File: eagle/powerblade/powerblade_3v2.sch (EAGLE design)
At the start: 78 parts, among them J1 JTAG_14PIN_IDC-ND, J2 AC_INF3, J4 TC2030-JLINK-NL, Q1 NTS4173, Q4 2SK1829, U1 TPS62122, U2 MCP6V3, U3 MSP430FR5738, U4 NRF51822QF, U6 MAX9910, U7 OPA2369, X1 16MHz, X3 32.768kHz, Y1 UREACH_XTEND

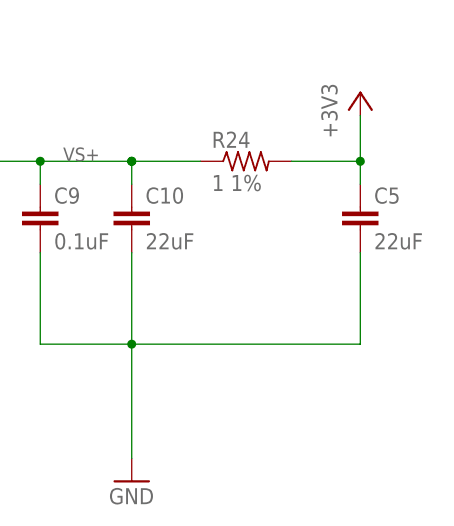
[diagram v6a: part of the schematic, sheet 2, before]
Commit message: updated most 0402 to new footprint
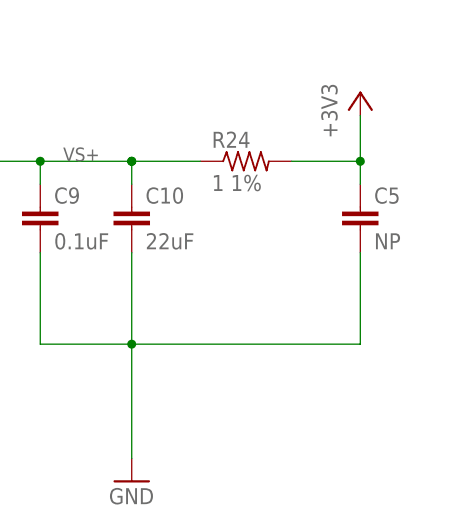
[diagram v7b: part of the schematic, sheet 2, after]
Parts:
- C11, C14, C16, C24, C27, C34, C38, C39, C4, C6, C7, C8: device rcl:C-EUC0402_SM -> rcl:C-EUC0402
- C5: value 22uF -> NP; DIGIKEY 445-9077-1-ND -> NP
- R14, R15, R16, R17, R18, R19, R35, R37, R38, R39, R40: device rcl:R-US_R0402_SM -> rcl:R-US_R0402
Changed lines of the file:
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@@
 <part name="GND3" library="supply1" deviceset="GND" device=""/>
 <part name="GND4" library="supply1" deviceset="GND" device=""/>
-<part name="C4" library="rcl" deviceset="C-EU" device="C0402_SM" value="22pF">
+<part name="C4" library="rcl" deviceset="C-EU" device="C0402" value="22pF">
 <attribute name="DIGIKEY" value="445-1239-1-ND"/>
 </part>
 <part name="P+2" library="supply1" deviceset="VCC" device=""/>
-<part name="C7" library="rcl" deviceset="C-EU" device="C0402_SM" value="4.7uF">
+<part name="C7" library="rcl" deviceset="C-EU" device="C0402" value="4.7uF">
 <attribute name="DIGIKEY" value="445-8023-1-ND"/>
 </part>
-<part name="C8" library="rcl" deviceset="C-EU" device="C0402_SM" value="0.1uF">
+<part name="C8" library="rcl" deviceset="C-EU" device="C0402" value="0.1uF">
 <attribute name="DIGIKEY" value="445-4952-1-ND"/>
 </part>
@@
 <attribute name="DIGIKEY" value="732-3452-1-ND"/>
 </part>
-<part name="R14" library="rcl" deviceset="R-US_" device="R0402_SM" value="200">
+<part name="R14" library="rcl" deviceset="R-US_" device="R0402" value="200">
 <attribute name="DIGIKEY" value="P200LCT-ND"/>
 </part>
-<part name="R15" library="rcl" deviceset="R-US_" device="R0402_SM" value="1M 1%">
-<attribute name="DIGIKEY" value="P1.00MLCT-ND"/>
-</part>
-<part name="R16" library="rcl" deviceset="R-US_" device="R0402_SM" value="75 1%">
+<part name="R15" library="rcl" deviceset="R-US_" device="R0402" value="1M 1%">
+<attribute name="DIGIKEY" value="P1.00MLCT-ND"/>
+</part>
+<part name="R16" library="rcl" deviceset="R-US_" device="R0402" value="75 1%">
 <attribute name="DIGIKEY" value="P75.0LCT-ND"/>
 </part>
-<part name="R17" library="rcl" deviceset="R-US_" device="R0402_SM" value="4.99k 1%">
+<part name="R17" library="rcl" deviceset="R-US_" device="R0402" value="4.99k 1%">
 <attribute name="DIGIKEY" value="P4.99KLCT-ND"/>
 <attribute name="DIGIKEY_2" value="P10.0KLCT-ND"/>
 </part>
-<part name="R18" library="rcl" deviceset="R-US_" device="R0402_SM" value="4.99 1%">
+<part name="R18" library="rcl" deviceset="R-US_" device="R0402" value="4.99 1%">
 <attribute name="DIGIKEY" value="RMCF0402FT4R99CT-ND"/>
 <attribute name="DIGIKEY_2" value="P10.0LCT-ND"/>
 </part>
-<part name="C27" library="rcl" deviceset="C-EU" device="C0402_SM" value="0.1uF">
+<part name="C27" library="rcl" deviceset="C-EU" device="C0402" value="0.1uF">
 <attribute name="DIGIKEY" value="445-4952-1-ND"/>
 </part>
@@
 <part name="+3V8" library="supply1" deviceset="+3V3" device=""/>
 <part name="U7" library="powerfilm" deviceset="OPA2369" device=""/>
-<part name="C38" library="rcl" deviceset="C-EU" device="C0402_SM" value="0.1uF">
+<part name="C38" library="rcl" deviceset="C-EU" device="C0402" value="0.1uF">
 <attribute name="DIGIKEY" value="445-4952-1-ND"/>
 </part>
 <part name="+3V3" library="supply1" deviceset="+3V3" device=""/>
-<part name="R35" library="rcl" deviceset="R-US_" device="R0402_SM" value="20k">
+<part name="R35" library="rcl" deviceset="R-US_" device="R0402" value="20k">
 <attribute name="DIGIKEY" value="P2.00KLCT-ND"/>
 <attribute name="DIGIKEY_2" value="P20.0KLCT-ND"/>
 </part>
-<part name="R37" library="rcl" deviceset="R-US_" device="R0402_SM" value="887k 1%">
+<part name="R37" library="rcl" deviceset="R-US_" device="R0402" value="887k 1%">
 <attribute name="DIGIKEY" value="P887KLCT-ND"/>
 </part>
-<part name="R38" library="rcl" deviceset="R-US_" device="R0402_SM" value="30k 1%">
+<part name="R38" library="rcl" deviceset="R-US_" device="R0402" value="30k 1%">
 <attribute name="DIGIKEY" value="P30.0KLCT-ND"/>
 </part>
-<part name="R40" library="rcl" deviceset="R-US_" device="R0402_SM" value="1M 1%">
-<attribute name="DIGIKEY" value="P1.00MLCT-ND"/>
-</part>
-<part name="C39" library="rcl" deviceset="C-EU" device="C0402_SM" value="1.5uF">
+<part name="R40" library="rcl" deviceset="R-US_" device="R0402" value="1M 1%">
+<attribute name="DIGIKEY" value="P1.00MLCT-ND"/>
+</part>
+<part name="C39" library="rcl" deviceset="C-EU" device="C0402" value="1.5uF">
 <attribute name="DIGIKEY" value="445-13815-1-ND"/>
 </part>
-<part name="R39" library="rcl" deviceset="R-US_" device="R0402_SM" value="16k 1%">
+<part name="R39" library="rcl" deviceset="R-US_" device="R0402" value="16k 1%">
 <attribute name="DIGIKEY" value="P16.0KLCT-ND"/>
 </part>
@@
 </part>
 <part name="U3" library="powerfilm" deviceset="MSP430FR5738" device=""/>
-<part name="C14" library="rcl" deviceset="C-EU" device="C0402_SM" value="0.1uF">
+<part name="C14" library="rcl" deviceset="C-EU" device="C0402" value="0.1uF">
 <attribute name="DIGIKEY" value="445-4952-1-ND"/>
 </part>
@@
 <attribute name="DIGIKEY" value="445-6853-1-ND"/>
 </part>
-<part name="C16" library="rcl" deviceset="C-EU" device="C0402_SM" value="470nF">
+<part name="C16" library="rcl" deviceset="C-EU" device="C0402" value="470nF">
 <attribute name="DIGIKEY" value="445-4989-1-ND"/>
 </part>
@@
 <part name="GND21" library="supply1" deviceset="GND" device=""/>
 <part name="+3V4" library="supply1" deviceset="+3V3" device=""/>
-<part name="R19" library="rcl" deviceset="R-US_" device="R0402_SM" value="47k">
+<part name="R19" library="rcl" deviceset="R-US_" device="R0402" value="47k">
 <attribute name="DIGIKEY" value="P47KJCT-ND"/>
 </part>
@@
 <attribute name="DIGIKEY" value="535-12373-1-ND"/>
 </part>
-<part name="C6" library="rcl" deviceset="C-EU" device="C0402_SM" value="8pF">
+<part name="C6" library="rcl" deviceset="C-EU" device="C0402" value="8pF">
 <attribute name="DIGIKEY" value="445-4890-1-ND"/>
 </part>
-<part name="C34" library="rcl" deviceset="C-EU" device="C0402_SM" value="8pF">
+<part name="C34" library="rcl" deviceset="C-EU" device="C0402" value="8pF">
 <attribute name="DIGIKEY" value="445-4890-1-ND"/>
 </part>
@@
 <attribute name="DIGIKEY_2" value="478-8654-1-ND"/>
 </part>
-<part name="C5" library="rcl" deviceset="C-EU" device="C0603_TN" value="22uF">
-<attribute name="DIGIKEY" value="445-9077-1-ND"/>
+<part name="C5" library="rcl" deviceset="C-EU" device="C0603_TN" value="NP">
+<attribute name="DIGIKEY" value="NP"/>
 </part>
 <part name="Y1" library="powerfilm" deviceset="UREACH_XTEND" device=""/>
-<part name="C24" library="rcl" deviceset="C-EU" device="C0402_SM" value="0.1uF">
-<attribute name="DIGIKEY" value="445-4952-1-ND"/>
-</part>
-<part name="C11" library="rcl" deviceset="C-EU" device="C0402_SM" value="4.7uF">
+<part name="C24" library="rcl" deviceset="C-EU" device="C0402" value="0.1uF">
+<attribute name="DIGIKEY" value="445-4952-1-ND"/>
+</part>
+<part name="C11" library="rcl" deviceset="C-EU" device="C0402" value="4.7uF">
 <attribute name="DIGIKEY" value="445-5947-1-ND"/>
 </part>

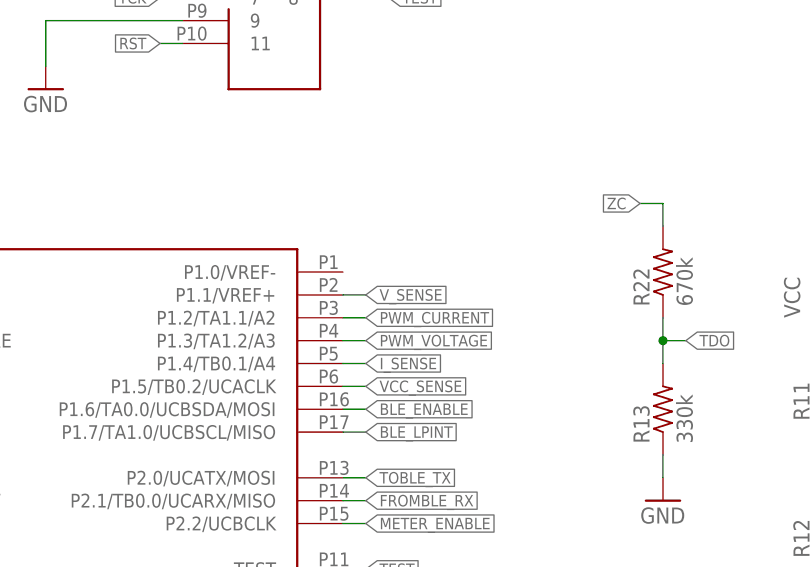
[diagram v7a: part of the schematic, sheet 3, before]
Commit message: finished routing in powerblade incl vfilt
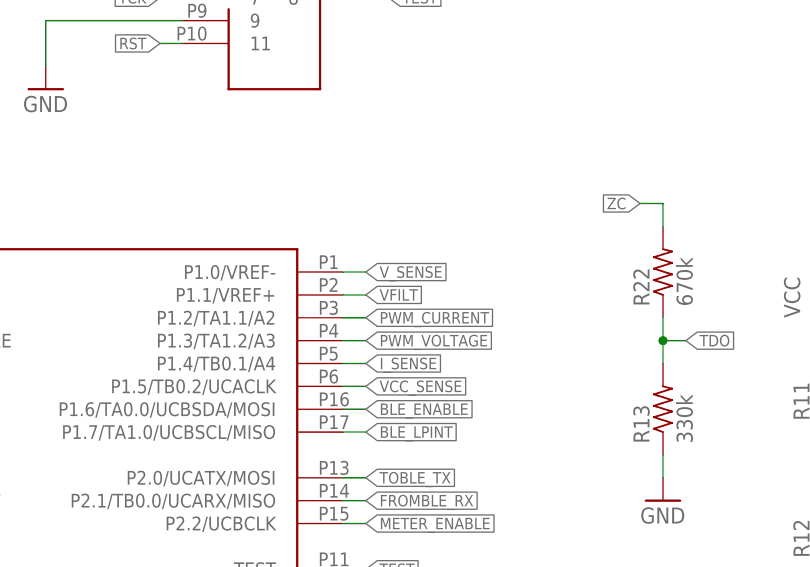
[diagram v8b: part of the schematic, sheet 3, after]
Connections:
- net VFILT: now also U3.P1.1/VREF+
- net V_SENSE: now also U3.P1.0/VREF-; no longer U3.P1.1/VREF+
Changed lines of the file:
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@@
 <grid distance="0.1" unitdist="inch" unit="inch" style="lines" multiple="1" display="no" altdistance="0.01" altunitdist="inch" altunit="inch"/>
 <layers>
-<layer number="1" name="Top" color="4" fill="1" visible="yes" active="no"/>
-<layer number="2" name="Route2" color="1" fill="3" visible="yes" active="no"/>
-<layer number="3" name="Route3" color="4" fill="3" visible="yes" active="no"/>
-<layer number="4" name="Route4" color="1" fill="4" visible="yes" active="no"/>
-<layer number="5" name="Route5" color="4" fill="4" visible="yes" active="no"/>
-<layer number="6" name="Route6" color="1" fill="8" visible="yes" active="no"/>
-<layer number="7" name="Route7" color="4" fill="8" visible="yes" active="no"/>
-<layer number="8" name="Route8" color="1" fill="2" visible="yes" active="no"/>
-<layer number="9" name="Route9" color="4" fill="2" visible="yes" active="no"/>
-<layer number="10" name="Route10" color="1" fill="7" visible="yes" active="no"/>
-<layer number="11" name="Route11" color="4" fill="7" visible="yes" active="no"/>
-<layer number="12" name="Route12" color="1" fill="5" visible="yes" active="no"/>
-<layer number="13" name="Route13" color="4" fill="5" visible="yes" active="no"/>
-<layer number="14" name="Route14" color="1" fill="6" visible="yes" active="no"/>
-<layer number="15" name="Route15" color="4" fill="6" visible="yes" active="no"/>
-<layer number="16" name="Bottom" color="1" fill="1" visible="yes" active="no"/>
-<layer number="17" name="Pads" color="2" fill="1" visible="yes" active="no"/>
-<layer number="18" name="Vias" color="2" fill="1" visible="yes" active="no"/>
-<layer number="19" name="Unrouted" color="6" fill="1" visible="yes" active="no"/>
-<layer number="20" name="Dimension" color="15" fill="1" visible="yes" active="no"/>
-<layer number="21" name="tPlace" color="7" fill="1" visible="yes" active="no"/>
-<layer number="22" name="bPlace" color="7" fill="1" visible="yes" active="no"/>
-<layer number="23" name="tOrigins" color="15" fill="1" visible="yes" active="no"/>
-<layer number="24" name="bOrigins" color="15" fill="1" visible="yes" active="no"/>
-<layer number="25" name="tNames" color="7" fill="1" visible="yes" active="no"/>
-<layer number="26" name="bNames" color="7" fill="1" visible="yes" active="no"/>
-<layer number="27" name="tValues" color="7" fill="1" visible="yes" active="no"/>
-<layer number="28" name="bValues" color="7" fill="1" visible="yes" active="no"/>
+<layer number="1" name="Top" color="4" fill="1" visible="no" active="no"/>
+<layer number="2" name="Route2" color="1" fill="3" visible="no" active="no"/>
+<layer number="3" name="Route3" color="4" fill="3" visible="no" active="no"/>
+<layer number="4" name="Route4" color="1" fill="4" visible="no" active="no"/>
+<layer number="5" name="Route5" color="4" fill="4" visible="no" active="no"/>
+<layer number="6" name="Route6" color="1" fill="8" visible="no" active="no"/>
+<layer number="7" name="Route7" color="4" fill="8" visible="no" active="no"/>
+<layer number="8" name="Route8" color="1" fill="2" visible="no" active="no"/>
+<layer number="9" name="Route9" color="4" fill="2" visible="no" active="no"/>
+<layer number="10" name="Route10" color="1" fill="7" visible="no" active="no"/>
+<layer number="11" name="Route11" color="4" fill="7" visible="no" active="no"/>
+<layer number="12" name="Route12" color="1" fill="5" visible="no" active="no"/>
+<layer number="13" name="Route13" color="4" fill="5" visible="no" active="no"/>
+<layer number="14" name="Route14" color="1" fill="6" visible="no" active="no"/>
+<layer number="15" name="Route15" color="4" fill="6" visible="no" active="no"/>
+<layer number="16" name="Bottom" color="1" fill="1" visible="no" active="no"/>
+<layer number="17" name="Pads" color="2" fill="1" visible="no" active="no"/>
+<layer number="18" name="Vias" color="2" fill="1" visible="no" active="no"/>
+<layer number="19" name="Unrouted" color="6" fill="1" visible="no" active="no"/>
+<layer number="20" name="Dimension" color="15" fill="1" visible="no" active="no"/>
+<layer number="21" name="tPlace" color="7" fill="1" visible="no" active="no"/>
+<layer number="22" name="bPlace" color="7" fill="1" visible="no" active="no"/>
+<layer number="23" name="tOrigins" color="15" fill="1" visible="no" active="no"/>
+<layer number="24" name="bOrigins" color="15" fill="1" visible="no" active="no"/>
+<layer number="25" name="tNames" color="7" fill="1" visible="no" active="no"/>
+<layer number="26" name="bNames" color="7" fill="1" visible="no" active="no"/>
+<layer number="27" name="tValues" color="7" fill="1" visible="no" active="no"/>
+<layer number="28" name="bValues" color="7" fill="1" visible="no" active="no"/>
 <layer number="29" name="tStop" color="7" fill="3" visible="no" active="no"/>
 <layer number="30" name="bStop" color="7" fill="6" visible="no" active="no"/>
@@
 <layer number="35" name="tGlue" color="7" fill="4" visible="no" active="no"/>
 <layer number="36" name="bGlue" color="7" fill="5" visible="no" active="no"/>
-<layer number="37" name="tTest" color="7" fill="1" visible="yes" active="no"/>
-<layer number="38" name="bTest" color="7" fill="1" visible="yes" active="no"/>
+<layer number="37" name="tTest" color="7" fill="1" visible="no" active="no"/>
+<layer number="38" name="bTest" color="7" fill="1" visible="no" active="no"/>
 <layer number="39" name="tKeepout" color="4" fill="11" visible="no" active="no"/>
 <layer number="40" name="bKeepout" color="1" fill="11" visible="no" active="no"/>
@@
 <layer number="44" name="Drills" color="7" fill="1" visible="no" active="no"/>
 <layer number="45" name="Holes" color="7" fill="1" visible="no" active="no"/>
-<layer number="46" name="Milling" color="3" fill="1" visible="yes" active="no"/>
-<layer number="47" name="Measures" color="7" fill="1" visible="yes" active="no"/>
-<layer number="48" name="Document" color="7" fill="1" visible="yes" active="no"/>
-<layer number="49" name="Reference" color="7" fill="1" visible="yes" active="no"/>
-<layer number="50" name="dxf" color="7" fill="1" visible="yes" active="no"/>
-<layer number="51" name="tDocu" color="7" fill="1" visible="yes" active="no"/>
-<layer number="52" name="bDocu" color="7" fill="1" visible="yes" active="no"/>
-<layer number="53" name="tGND_GNDA" color="7" fill="9" visible="yes" active="no"/>
-<layer number="54" name="bGND_GNDA" color="1" fill="9" visible="yes" active="no"/>
-<layer number="56" name="wert" color="7" fill="1" visible="yes" active="no"/>
-<layer number="57" name="tCAD" color="7" fill="1" visible="yes" active="no"/>
+<layer number="46" name="Milling" color="3" fill="1" visible="no" active="no"/>
+<layer number="47" name="Measures" color="7" fill="1" visible="no" active="no"/>
+<layer number="48" name="Document" color="7" fill="1" visible="no" active="no"/>
+<layer number="49" name="Reference" color="7" fill="1" visible="no" active="no"/>
+<layer number="50" name="dxf" color="7" fill="1" visible="no" active="no"/>
+<layer number="51" name="tDocu" color="7" fill="1" visible="no" active="no"/>
+<layer number="52" name="bDocu" color="7" fill="1" visible="no" active="no"/>
+<layer number="53" name="tGND_GNDA" color="7" fill="9" visible="no" active="no"/>
+<layer number="54" name="bGND_GNDA" color="1" fill="9" visible="no" active="no"/>
+<layer number="56" name="wert" color="7" fill="1" visible="no" active="no"/>
+<layer number="57" name="tCAD" color="7" fill="1" visible="no" active="no"/>
 <layer number="91" name="Nets" color="2" fill="1" visible="yes" active="yes"/>
 <layer number="92" name="Busses" color="1" fill="1" visible="yes" active="yes"/>
@@
 <net name="V_SENSE" class="0">
 <segment>
-<label x="27.94" y="15.24" size="1.27" layer="95" xref="yes"/>
-<pinref part="U3" gate="G$1" pin="P1.1/VREF+"/>
-<wire x1="25.4" y1="15.24" x2="27.94" y2="15.24" width="0.1524" layer="91"/>
+<label x="27.94" y="17.78" size="1.27" layer="95" xref="yes"/>
+<pinref part="U3" gate="G$1" pin="P1.0/VREF-"/>
+<wire x1="25.4" y1="17.78" x2="27.94" y2="17.78" width="0.1524" layer="91"/>
 </segment>
 </net>
@@
 </segment>
 </net>
+<net name="VFILT" class="0">
+<segment>
+<pinref part="U3" gate="G$1" pin="P1.1/VREF+"/>
+<wire x1="27.94" y1="15.24" x2="25.4" y2="15.24" width="0.1524" layer="91"/>
+<label x="27.94" y="15.24" size="1.27" layer="95" xref="yes"/>
+</segment>
+</net>
